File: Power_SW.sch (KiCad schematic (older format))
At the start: 95 parts, among them J9 Conn_01x04_Male, Q10 FDMS7608S, Q11 FDMS7608S, Q12 FDMS7608S, Q13 FDMS7608S, Q26 BC847BV, Q27 BC847BV, U35 XRP7724ILB-F, U36 NCP186AMX180TAG, U37 NCP186AMX120TAG

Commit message: SW2 placement changed, BOM cleared, FPGA boot, less ERC errors and wornings
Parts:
- D2, D5: footprint SOD2512X110N -> ICs And Semiconductors SMD:SOD2512X110N
- R189, R196: config (none) -> dnf
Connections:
- wire segments 299 -> 307
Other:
- moved on the sheet: R190, R191, R192, R194

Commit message: BOM updated, 25MHz clock level fixed
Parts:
- J9: symbol AMC_FMC_Carrier-PcbDoc-rescue:Conn_01x04_Male-Connector -> AMC_FMC_Carrier-PcbDoc-rescue:Conn_01x04_Male-Connector-AMC_FMC_Carrier-PcbDoc-rescue
- U36, U37: symbol AMC_FMC_Carrier-PcbDoc-rescue:NCP186AMX120TAG-powerMG -> AMC_FMC_Carrier-PcbDoc-rescue:NCP186AMX120TAG-powerMG-AMC_FMC_Carrier-PcbDoc-rescue
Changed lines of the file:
@@
 	6150 1050 6150 1700
 $Comp
-L AMC_FMC_Carrier-PcbDoc-rescue:Conn_01x04_Male-Connector J?
+L AMC_FMC_Carrier-PcbDoc-rescue:Conn_01x04_Male-Connector-AMC_FMC_Carrier-PcbDoc-rescue J?
 U 1 1 5DBB4777
 P 3900 2700
@@
 $EndComp
 $Comp
-L AMC_FMC_Carrier-PcbDoc-rescue:VCCAUX-powerMG #PWR?
+L AMC_FMC_Carrier-PcbDoc-rescue:VCCAUX-powerMG-AMC_FMC_Carrier-PcbDoc-rescue #PWR?
 U 1 1 5DBB8165
 P 9050 7950
@@
 $EndComp
 $Comp
-L AMC_FMC_Carrier-PcbDoc-rescue:VCCBRAM-powerMG #PWR?
+L AMC_FMC_Carrier-PcbDoc-rescue:VCCBRAM-powerMG-AMC_FMC_Carrier-PcbDoc-rescue #PWR?
 U 1 1 5DBB816B
 P 15300 7600
@@
 $EndComp
 $Comp
-L AMC_FMC_Carrier-PcbDoc-rescue:MGTAVCC-powerMG #PWR?
+L AMC_FMC_Carrier-PcbDoc-rescue:MGTAVCC-powerMG-AMC_FMC_Carrier-PcbDoc-rescue #PWR?
 U 1 1 5DBB8171
 P 15650 7600
@@
 	12650 2350 13550 2350
 $Comp
-L AMC_FMC_Carrier-PcbDoc-rescue:NCP186AMX120TAG-powerMG U?
+L AMC_FMC_Carrier-PcbDoc-rescue:NCP186AMX120TAG-powerMG-AMC_FMC_Carrier-PcbDoc-rescue U?
 U 1 1 5DBB8221
 P 6650 7700
@@
 Connection ~ 7950 10000
 $Comp
-L AMC_FMC_Carrier-PcbDoc-rescue:NCP186AMX120TAG-powerMG U?
+L AMC_FMC_Carrier-PcbDoc-rescue:NCP186AMX120TAG-powerMG-AMC_FMC_Carrier-PcbDoc-rescue U?
 U 1 1 5D300F70
 P 6650 9400
@@
 $EndComp
 $Comp
-L AMC_FMC_Carrier-PcbDoc-rescue:MGTAVTT-powerMG #PWR?
+L AMC_FMC_Carrier-PcbDoc-rescue:MGTAVTT-powerMG-AMC_FMC_Carrier-PcbDoc-rescue #PWR?
 U 1 1 5DBB815F
 P 9050 9650
@@
 NoConn ~ 7550 5100
 $Comp
-L AMC_FMC_Carrier-PcbDoc-rescue:MGTAVTT-powerMG #PWR?
+L AMC_FMC_Carrier-PcbDoc-rescue:MGTAVTT-powerMG-AMC_FMC_Carrier-PcbDoc-rescue #PWR?
 U 1 1 5CF3EE50
 P 3100 6450

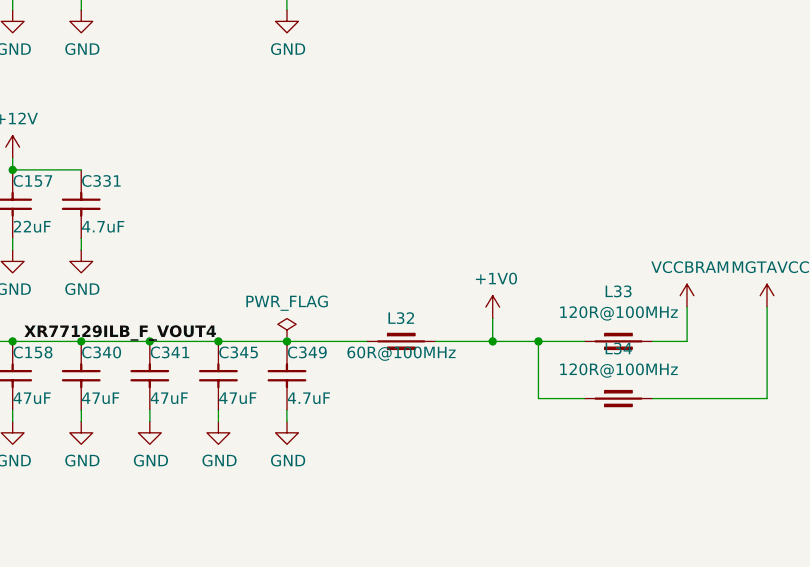
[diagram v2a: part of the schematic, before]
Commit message: one more Ferrit at 1V has beed added
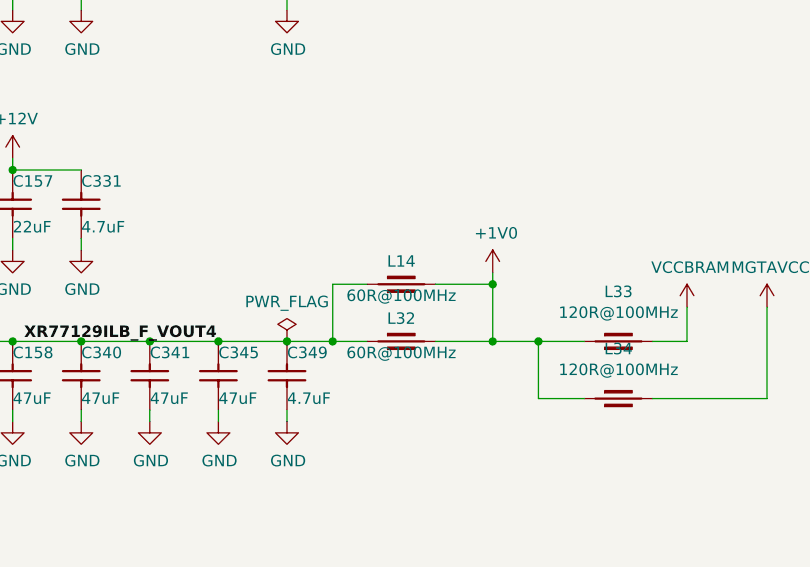
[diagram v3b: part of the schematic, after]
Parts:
- added L14: IND1806_MURATA_BLM41PG600SN1L, INDC4516X180N, symbol Inductors_SMD:IND1806_MURATA_BLM41PG600SN1L
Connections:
- wire segments 307 -> 312
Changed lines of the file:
@@
 L power:+1V0 #PWR?
 U 1 1 5DBB7E73
-P 14450 7650
+P 14450 7450
 AR Path="/5C16BF8E/5DBB7E73" Ref="#PWR?"  Part="1"
 AR Path="/5C16BF8E/5DB9B7E6/5DBB7E73" Ref="#PWR0542"  Part="1"
-F 0 "#PWR0542" H 14450 7500 50  0001 C CNN
-F 1 "+1V0" H 14465 7823 50  0000 C CNN
-F 2 "" H 14450 7650 50  0001 C CNN
-F 3 "" H 14450 7650 50  0001 C CNN
-	1    14450 7650
+F 0 "#PWR0542" H 14450 7300 50  0001 C CNN
+F 1 "+1V0" H 14465 7623 50  0000 C CNN
+F 2 "" H 14450 7450 50  0001 C CNN
+F 3 "" H 14450 7450 50  0001 C CNN
+	1    14450 7450
 	1    0    0    -1
 $EndComp
@@
 1V2
 Wire Wire Line
-	14450 7750 14450 7650
-Wire Wire Line
 	14650 8000 14850 8000
 Connection ~ 14450 7750
@@
 Connection ~ 13550 7750
 Wire Wire Line
-	13550 7750 13900 7750
+	13550 7750 13750 7750
 Connection ~ 13550 5950
 Wire Wire Line
@@
 	1    0    0    1
 $EndComp
+$Comp
+L Inductors_SMD:IND1806_MURATA_BLM41PG600SN1L L14
+U 1 1 5CF9305C
+P 13900 7500
+F 0 "L14" H 14050 7600 50  0000 C CNN
+F 1 "IND1806_MURATA_BLM41PG600SN1L" H 13900 7310 60  0001 L CNN
+F 2 "INDC4516X180N" H 13900 6500 60  0001 L CNN
+F 3 "\\\\cern.ch\\dfs\\Applications\\Altium\\Datasheets\\IND1806_MURATA_BLM41P.pdf" H 13900 7130 60  0001 L CNN
+F 4 "60R@100MHz" H 14050 7450 50  0000 C CNN "~"
+F 5 "IND1806_MURATA_BLM41PG600SN1L" H 13900 7040 60  0001 L CNN "Part Number"
+F 6 "Inductor" H 13900 6950 60  0001 L CNN "Library Ref"
+F 7 "SchLib\\Inductors & Transformers.SchLib" H 13900 6860 60  0001 L CNN "Library Path"
+F 8 "=Value" H 13900 6770 60  0001 L CNN "Comment"
+F 9 "Standard" H 13900 6680 60  0001 L CNN "Component Kind"
+F 10 "Standard" H 13900 6590 60  0001 L CNN "Component Type"
+F 11 "~~" H 13900 6410 60  0001 L CNN "PackageDescription"
+F 12 "2.0000000000000000e+00" H 13900 6320 60  0001 L CNN "Pin Count"
+F 13 "PcbLib\\Inductors SMD.PcbLib" H 13900 6230 60  0001 L CNN "Footprint Path"
+F 14 "INDC4516X180N" H 13900 6140 60  0001 L CNN "Footprint Ref"
+F 15 "60R@100MHz" H 13900 6050 60  0001 L CNN "Val"
+F 16 "None" H 13900 5960 60  0001 L CNN "Status"
+F 17 "6A" H 13900 5870 60  0001 L CNN "Power"
+F 18 "0.01R" H 13900 5780 60  0001 L CNN "Resistance"
+F 19 "~~" H 13900 5690 60  0001 L CNN "Tolerance"
+F 20 "SMD EMI Suppression Chip Ferrite Bead (BLM41P Series)" H 13900 5600 60  0001 L CNN "Part Description"
+F 21 "MURATA" H 13900 5510 60  0001 L CNN "Manufacturer"
+F 22 "BLM41PG600SN1L" H 13900 5420 60  0001 L CNN "Manufacturer Part Number"
+F 23 "1806" H 13900 5330 60  0001 L CNN "Case"
+F 24 "Yes" H 13900 5240 60  0001 L CNN "Mounted"
+F 25 "No" H 13900 5150 60  0001 L CNN "Socket"
+F 26 "Yes" H 13900 5060 60  0001 L CNN "SMD"
+F 27 "~~" H 13900 4970 60  0001 L CNN "Sense Comment"
+F 28 "No" H 13900 4880 60  0001 L CNN "Sense"
+F 29 "~~" H 13900 4790 60  0001 L CNN "Status Comment"
+F 30 "1.8mm" H 13900 4700 60  0001 L CNN "ComponentHeight"
+F 31 "\\\\cern.ch\\dfs\\Applications\\Altium\\Datasheets\\IND1806_MURATA_BLM41P.pdf" H 13900 4610 60  0001 L CNN "HelpURL"
+F 32 "CERN DEM JLC" H 13900 4520 60  0001 L CNN "Author"
+F 33 "12/02/09 00:00:00" H 13900 4430 60  0001 L CNN "CreateDate"
+F 34 "12/02/09 00:00:00" H 13900 4340 60  0001 L CNN "LatestRevisionDate"
+F 35 "Inductors SMD" H 13900 4250 60  0001 L CNN "Library Name"
+F 36 "This work is licensed under the Creative Commons CC-BY-SA 4.0 License. To the extent that circuit schematics that use Licensed Material can be considered to be ‘Adapted Material’, then the copyright holder waives article 3.b of the license with respect to these schematics." H 13900 4160 60  0001 L CNN "License"
+	1    13900 7500
+	1    0    0    -1
+$EndComp
+Wire Wire Line
+	14450 7450 14450 7500
+Wire Wire Line
+	14200 7500 14450 7500
+Connection ~ 14450 7500
+Wire Wire Line
+	14450 7500 14450 7750
+Wire Wire Line
+	13900 7500 13750 7500
+Wire Wire Line
+	13750 7500 13750 7750
+Connection ~ 13750 7750
+Wire Wire Line
+	13750 7750 13900 7750
 $EndSCHEMATC

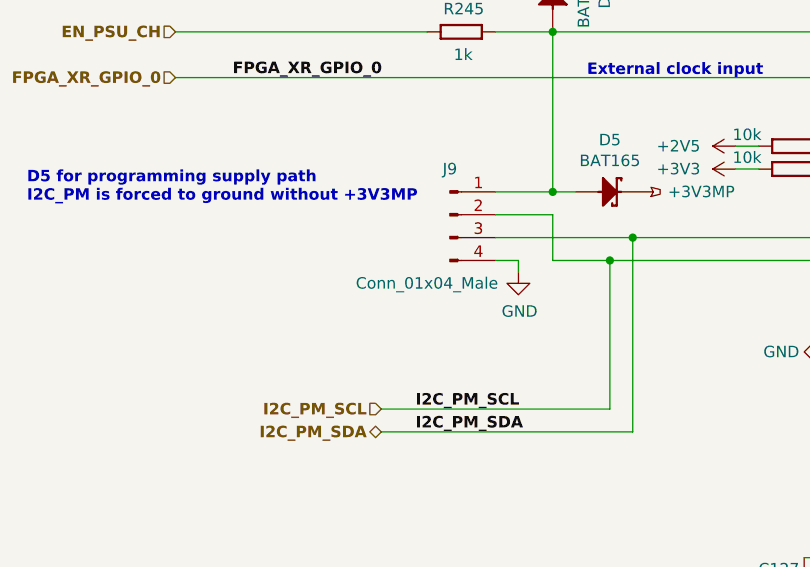
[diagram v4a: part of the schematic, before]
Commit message: BOM configuration file edited, updated Marble picture, some components part number changed
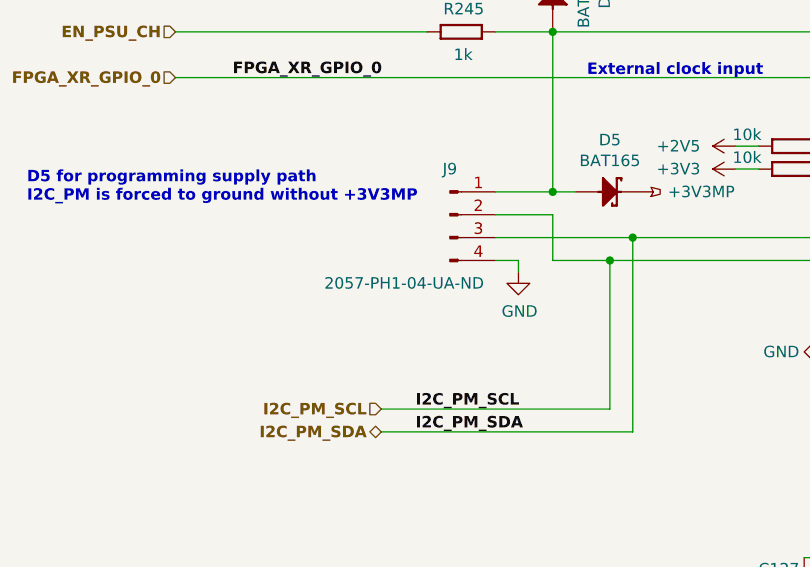
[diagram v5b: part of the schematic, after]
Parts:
- C151, C153, C155, C157: Manufacturer1 Example TDK -> Murata; Manufacturer1 Part Number C2012X5R1C226KT -> GRM21BR61C226ME44L
- D2, D5: Manufacturer Part Number BAT165 -> BAT165AX
- J9: value Conn_01x04_Male -> 2057-PH1-04-UA-ND; Manufacturer Part Number (none) -> 2057-PH1-04-UA-ND; PN MTLW-104-07-L-S-250 -> (none)
- U36: Manufacturer Part Number (none) -> NCP186AMX180TAG; PN NCP186AMX180TAG -> (none)
- U37: Manufacturer Part Number (none) -> NCP186AMX120TAG; PN NCP186AMX120TAG -> (none)
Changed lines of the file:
@@
 AR Path="/5C16BF8E/5DB9B7E6/5DBB4777" Ref="J9"  Part="1"
 F 0 "J9" H 3900 2900 50  0000 C CNN
-F 1 "Conn_01x04_Male" H 3800 2400 50  0000 C CNN
+F 1 "2057-PH1-04-UA-ND" H 3700 2400 50  0000 C CNN
 F 2 "Connectors THD:SAMTEC_MTLW-104-07-L-S-250" H 3900 2700 50  0001 C CNN
 F 3 "~" H 3900 2700 50  0001 C CNN
-F 4 "MTLW-104-07-L-S-250" H 3900 2700 50  0001 C CNN "PN"
+F 4 "2057-PH1-04-UA-ND" H 3900 2700 50  0001 C CNN "Manufacturer Part Number"
 	1    3900 2700
 	1    0    0    -1
@@
 F 30 "~~" H 12350 -1270 60  0001 L CNN "Sense Comment"
 F 31 "~~" H 12350 -1360 60  0001 L CNN "ComponentHeight"
-F 32 "TDK" H 12350 -1450 60  0001 L CNN "Manufacturer1 Example"
-F 33 "C2012X5R1C226KT" H 12350 -1540 60  0001 L CNN "Manufacturer1 Part Number"
+F 32 "Murata" H 12350 -1450 60  0001 L CNN "Manufacturer1 Example"
+F 33 "GRM21BR61C226ME44L" H 12350 -1540 60  0001 L CNN "Manufacturer1 Part Number"
 F 34 "1.35mm" H 12350 -1630 60  0001 L CNN "Manufacturer1 ComponentHeight"
 F 35 "\\\\cern.ch\\dfs\\Applications\\Altium\\Datasheets\\CC0805_X5R_TDK_C.pdf" H 12350 -1720 60  0001 L CNN "HelpURL"
@@
 F 30 "~~" H 12350 530 60  0001 L CNN "Sense Comment"
 F 31 "~~" H 12350 440 60  0001 L CNN "ComponentHeight"
-F 32 "TDK" H 12350 350 60  0001 L CNN "Manufacturer1 Example"
-F 33 "C2012X5R1C226KT" H 12350 260 60  0001 L CNN "Manufacturer1 Part Number"
+F 32 "Murata" H 12350 350 60  0001 L CNN "Manufacturer1 Example"
+F 33 "GRM21BR61C226ME44L" H 12350 260 60  0001 L CNN "Manufacturer1 Part Number"
 F 34 "1.35mm" H 12350 170 60  0001 L CNN "Manufacturer1 ComponentHeight"
 F 35 "\\\\cern.ch\\dfs\\Applications\\Altium\\Datasheets\\CC0805_X5R_TDK_C.pdf" H 12350 80  60  0001 L CNN "HelpURL"
@@
 F 30 "~~" H 12350 2330 60  0001 L CNN "Sense Comment"
 F 31 "~~" H 12350 2240 60  0001 L CNN "ComponentHeight"
-F 32 "TDK" H 12350 2150 60  0001 L CNN "Manufacturer1 Example"
-F 33 "C2012X5R1C226KT" H 12350 2060 60  0001 L CNN "Manufacturer1 Part Number"
+F 32 "Murata" H 12350 2150 60  0001 L CNN "Manufacturer1 Example"
+F 33 "GRM21BR61C226ME44L" H 12350 2060 60  0001 L CNN "Manufacturer1 Part Number"
 F 34 "1.35mm" H 12350 1970 60  0001 L CNN "Manufacturer1 ComponentHeight"
 F 35 "\\\\cern.ch\\dfs\\Applications\\Altium\\Datasheets\\CC0805_X5R_TDK_C.pdf" H 12350 1880 60  0001 L CNN "HelpURL"
@@
 F 30 "~~" H 12350 4130 60  0001 L CNN "Sense Comment"
 F 31 "~~" H 12350 4040 60  0001 L CNN "ComponentHeight"
-F 32 "TDK" H 12350 3950 60  0001 L CNN "Manufacturer1 Example"
-F 33 "C2012X5R1C226KT" H 12350 3860 60  0001 L CNN "Manufacturer1 Part Number"
+F 32 "Murata" H 12350 3950 60  0001 L CNN "Manufacturer1 Example"
+F 33 "GRM21BR61C226ME44L" H 12350 3860 60  0001 L CNN "Manufacturer1 Part Number"
 F 34 "1.35mm" H 12350 3770 60  0001 L CNN "Manufacturer1 ComponentHeight"
 F 35 "\\\\cern.ch\\dfs\\Applications\\Altium\\Datasheets\\CC0805_X5R_TDK_C.pdf" H 12350 3680 60  0001 L CNN "HelpURL"
@@
 F 2 "AG5300_2:SOIC-8" H 6650 7700 50  0001 C CNN
 F 3 "" H 6650 7700 50  0001 C CNN
-F 4 "NCP186AMX180TAG" H 6650 7700 50  0001 C CNN "PN"
+F 4 "NCP186AMX180TAG" H 6650 7700 50  0001 C CNN "Manufacturer Part Number"
 	1    6650 7700
 	1    0    0    -1
@@
 F 2 "AG5300_2:SOIC-8" H 6650 9400 50  0001 C CNN
 F 3 "" H 6650 9400 50  0001 C CNN
-F 4 "NCP186AMX120TAG" H 6650 9400 50  0001 C CNN "PN"
+F 4 "NCP186AMX120TAG" H 6650 9400 50  0001 C CNN "Manufacturer Part Number"
 	1    6650 9400
 	1    0    0    -1
@@
 F 15 "Medium Power AF Schottky Diode" H 4350 310 60  0001 L CNN "Part Description"
 F 16 "INFINEON" H 4350 220 60  0001 L CNN "Manufacturer"
-F 17 "BAT165" H 4350 130 60  0001 L CNN "Manufacturer Part Number"
+F 17 "BAT165AX" H 4350 130 60  0001 L CNN "Manufacturer Part Number"
 F 18 "2" H 4350 40  60  0001 L CNN "Pin Count"
 F 19 "SOD323" H 4350 -50 60  0001 L CNN "Case"
@@
 F 15 "Medium Power AF Schottky Diode" H 4450 1010 60  0001 L CNN "Part Description"
 F 16 "INFINEON" H 4450 920 60  0001 L CNN "Manufacturer"
-F 17 "BAT165" H 4450 830 60  0001 L CNN "Manufacturer Part Number"
+F 17 "BAT165AX" H 4450 830 60  0001 L CNN "Manufacturer Part Number"
 F 18 "2" H 4450 740 60  0001 L CNN "Pin Count"
 F 19 "SOD323" H 4450 650 60  0001 L CNN "Case"

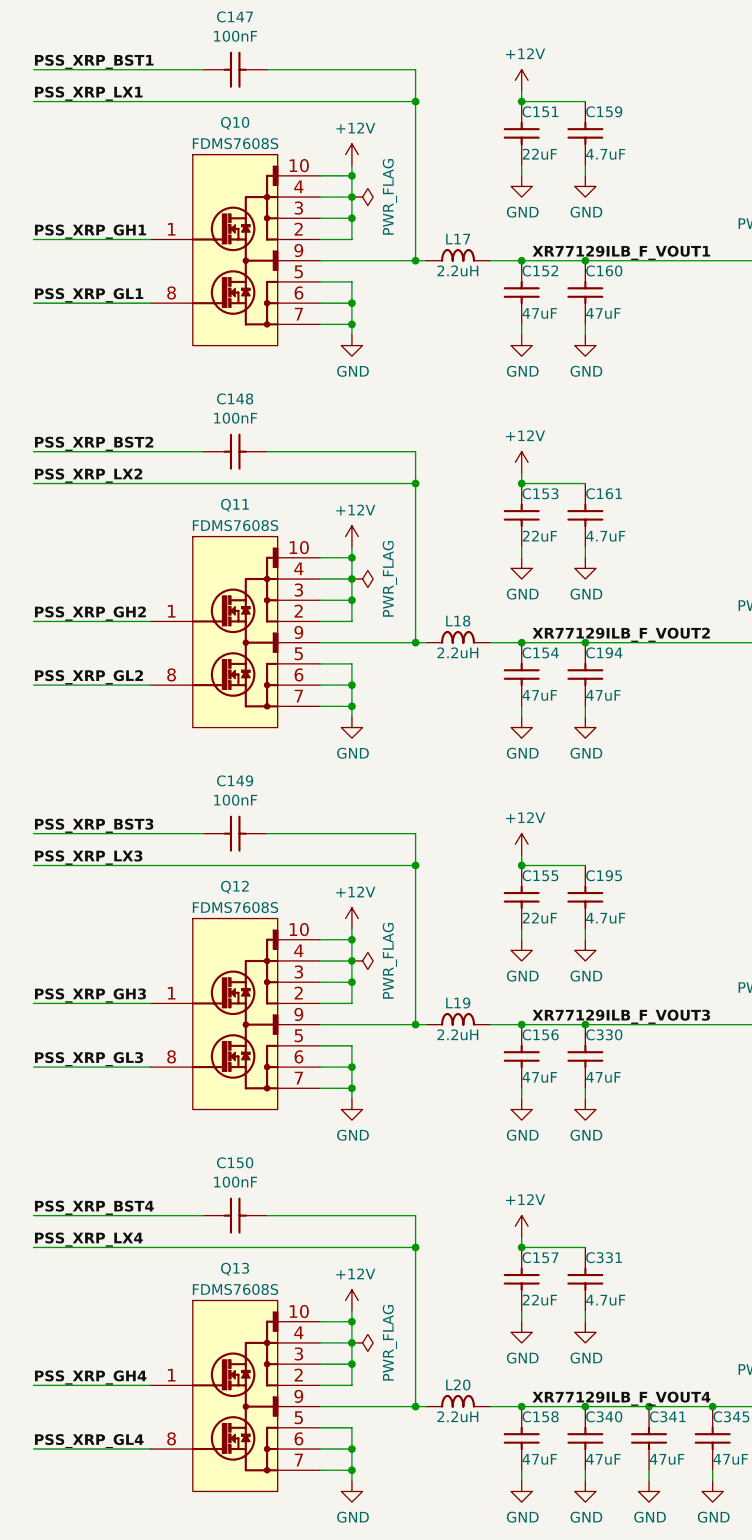
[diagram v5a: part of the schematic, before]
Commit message: README edited, less ERC errors and warnings
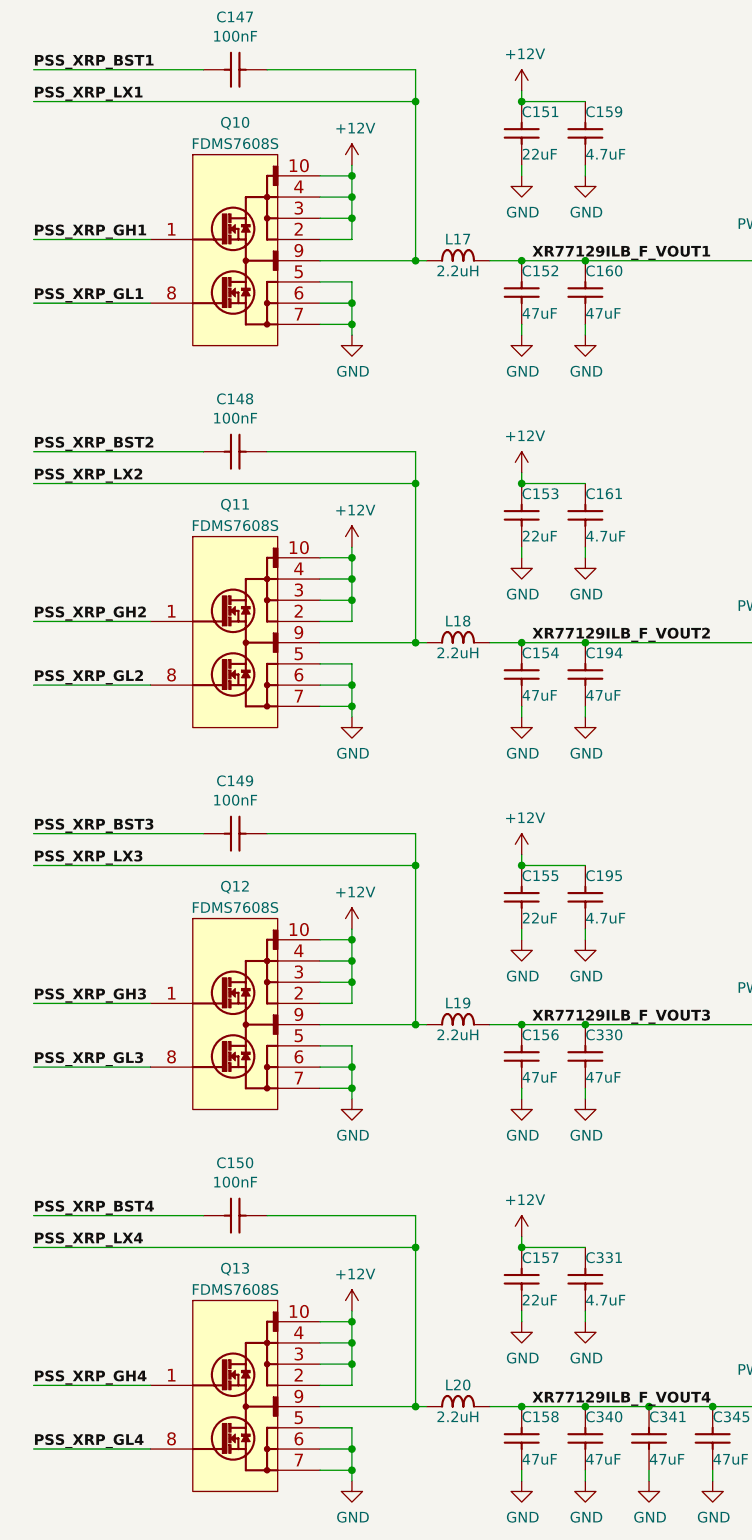
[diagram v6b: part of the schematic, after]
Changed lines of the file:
@@
-$Comp
-L power:PWR_FLAG #FLG?
-U 1 1 5D2256C5
-P 11550 3850
-AR Path="/5BABAC65/5D2256C5" Ref="#FLG?"  Part="1"
-AR Path="/5C16BF8E/5DB9B7E6/5D2256C5" Ref="#FLG0118"  Part="1"
-F 0 "#FLG0118" H 11550 3925 50  0001 C CNN
-F 1 "PWR_FLAG" H 11550 4023 50  0000 C CNN
-F 2 "" H 11550 3850 50  0001 C CNN
-F 3 "~" H 11550 3850 50  0001 C CNN
-	1    11550 3850
-	0    1    1    0
-$EndComp
-$Comp
-L power:PWR_FLAG #FLG?
-U 1 1 5D23EA53
-P 11550 2050
-AR Path="/5BABAC65/5D23EA53" Ref="#FLG?"  Part="1"
-AR Path="/5C16BF8E/5DB9B7E6/5D23EA53" Ref="#FLG0119"  Part="1"
-F 0 "#FLG0119" H 11550 2125 50  0001 C CNN
-F 1 "PWR_FLAG" H 11550 2223 50  0000 C CNN
-F 2 "" H 11550 2050 50  0001 C CNN
-F 3 "~" H 11550 2050 50  0001 C CNN
-	1    11550 2050
-	0    1    1    0
-$EndComp
-$Comp
-L power:PWR_FLAG #FLG?
-U 1 1 5D257CAE
-P 11550 5650
-AR Path="/5BABAC65/5D257CAE" Ref="#FLG?"  Part="1"
-AR Path="/5C16BF8E/5DB9B7E6/5D257CAE" Ref="#FLG0120"  Part="1"
-F 0 "#FLG0120" H 11550 5725 50  0001 C CNN
-F 1 "PWR_FLAG" H 11550 5823 50  0000 C CNN
-F 2 "" H 11550 5650 50  0001 C CNN
-F 3 "~" H 11550 5650 50  0001 C CNN
-	1    11550 5650
-	0    1    1    0
-$EndComp
-$Comp
-L power:PWR_FLAG #FLG?
-U 1 1 5D270EC0
-P 11550 7450
-AR Path="/5BABAC65/5D270EC0" Ref="#FLG?"  Part="1"
-AR Path="/5C16BF8E/5DB9B7E6/5D270EC0" Ref="#FLG0121"  Part="1"
-F 0 "#FLG0121" H 11550 7525 50  0001 C CNN
-F 1 "PWR_FLAG" H 11550 7623 50  0000 C CNN
-F 2 "" H 11550 7450 50  0001 C CNN
-F 3 "~" H 11550 7450 50  0001 C CNN
-	1    11550 7450
-	0    1    1    0
-$EndComp
 $Comp
 L power:PWR_FLAG #FLG?
